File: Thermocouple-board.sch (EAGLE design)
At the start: 107 parts, among them J1 RJ45, J10 1X2-3.5MM, J11 1X2-3.5MM, J12 1X2-3.5MM, J13 1X2-3.5MM, J2 RJ45, J20 HEADER-1X1, J21 HEADER-1X1, J22 HEADER-1X1, J3 1981584-1LONGPADS, J4 2.1MMJACKTHM, J5 ST-LINK, J6 HEADER-1X3, J7 UART, SW1 PUSHBUTTON, SW2 PUSHBUTTON, U1 STM32F042K6, U10 MAX31855, U11 MAX31855, U12 MAX31855, U13 MAX31855, U20 EEPROM-I2C, U21 EEPROM-I2C, U30 ST3485, U31 ST3485, U40 LP298XS, U70 TPS25921, Y1 8MHz

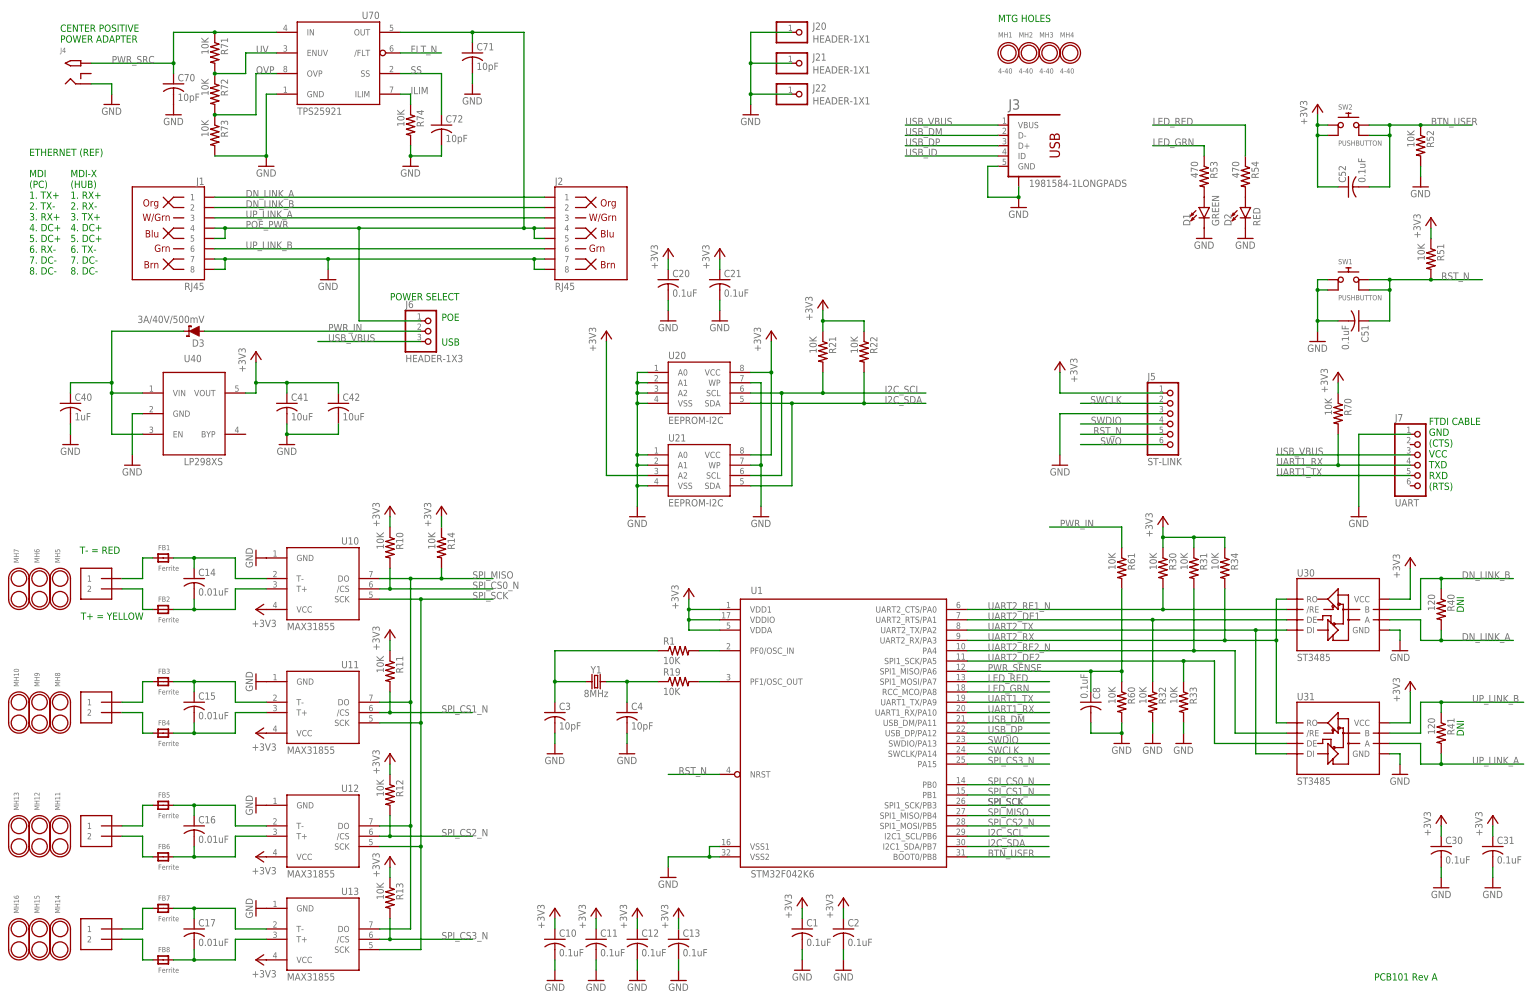
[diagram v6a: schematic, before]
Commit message: Update values on schematic
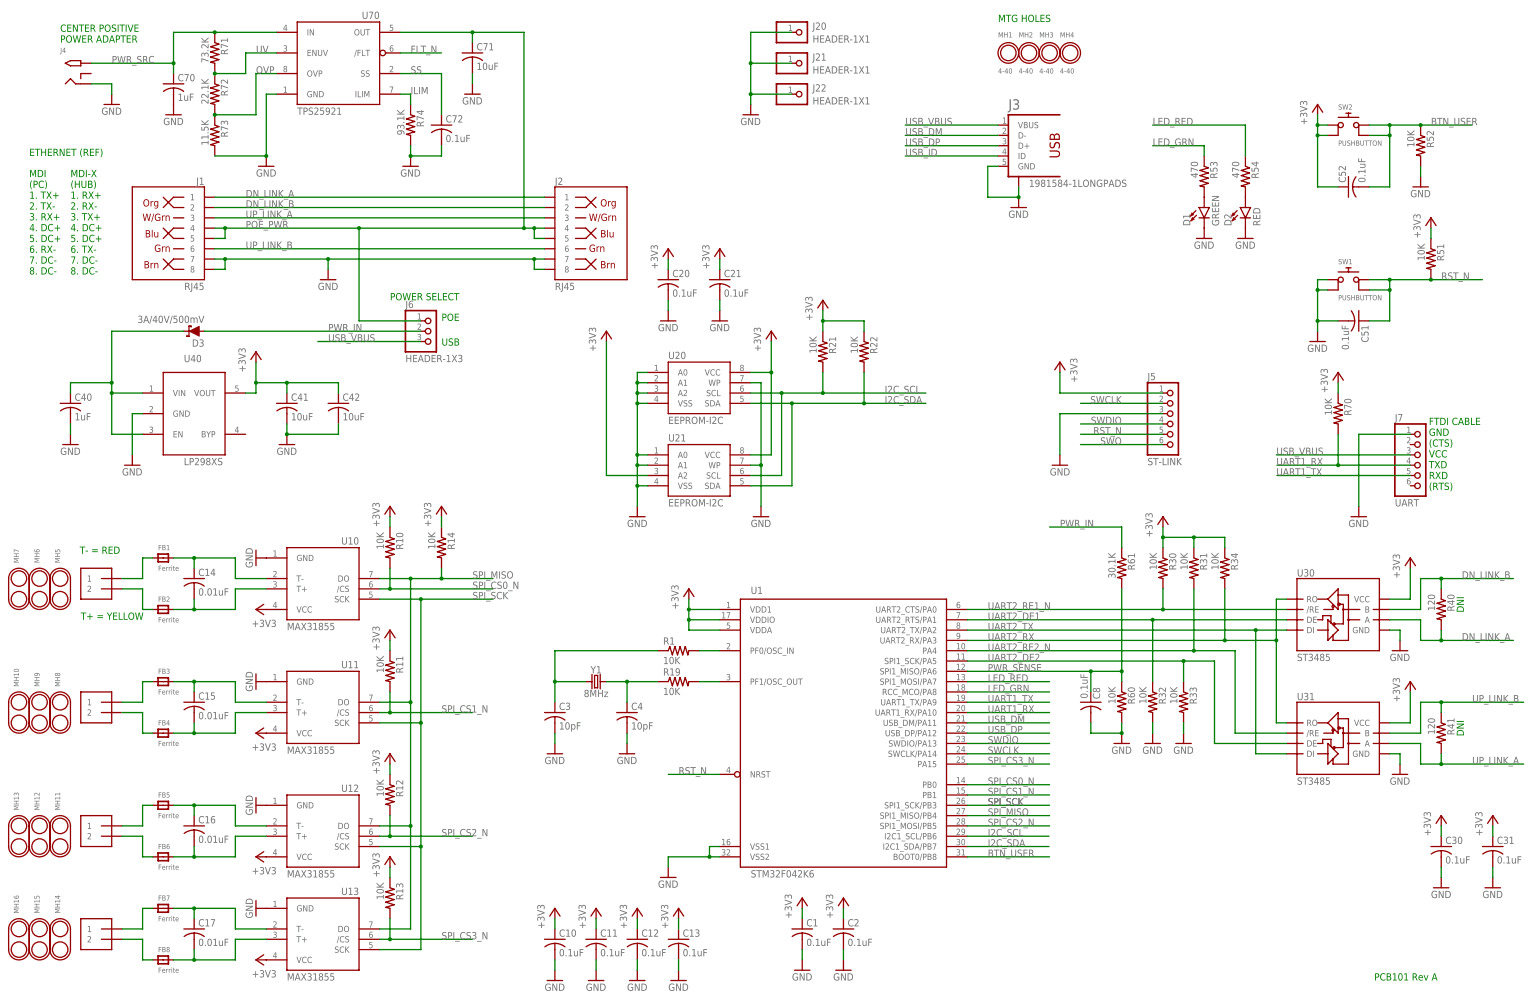
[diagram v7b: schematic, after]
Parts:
- C70: value 10pF -> 1uF
- C71: value 10pF -> 10uF
- C72: value 10pF -> 0.1uF
- R61: value 10K -> 30.1K
- R71: value 10K -> 73.2K
- R72: value 10K -> 22.1K
- R73: value 10K -> 11.5K
- R74: value 10K -> 93.1K
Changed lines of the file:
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@@
 <part name="MH4" library="Thermocouple-board" deviceset="MTG_HOLE" device="_4-40" value="4-40"/>
 <part name="R60" library="adafruit" deviceset="R-US_" device="R0805" value="10K"/>
-<part name="R61" library="adafruit" deviceset="R-US_" device="R0805" value="10K"/>
+<part name="R61" library="adafruit" deviceset="R-US_" device="R0805" value="30.1K"/>
 <part name="GND10" library="supply1" deviceset="GND" device=""/>
 <part name="C8" library="adafruit" library_urn="urn:adsk.eagle:library:420" deviceset="C-US" device="C0805K" package3d_urn="urn:adsk.eagle:package:6240397/1" value="0.1uF"/>
@@
 <part name="GND37" library="supply1" deviceset="GND" device=""/>
 <part name="GND38" library="supply1" deviceset="GND" device=""/>
-<part name="R71" library="adafruit" deviceset="R-US_" device="R0805" value="10K"/>
-<part name="R72" library="adafruit" deviceset="R-US_" device="R0805" value="10K"/>
-<part name="R73" library="adafruit" deviceset="R-US_" device="R0805" value="10K"/>
-<part name="R74" library="adafruit" deviceset="R-US_" device="R0805" value="10K"/>
-<part name="C72" library="adafruit" library_urn="urn:adsk.eagle:library:420" deviceset="C-US" device="C0805K" package3d_urn="urn:adsk.eagle:package:6240397/1" value="10pF"/>
-<part name="C71" library="adafruit" library_urn="urn:adsk.eagle:library:420" deviceset="C-US" device="C0805K" package3d_urn="urn:adsk.eagle:package:6240397/1" value="10pF"/>
+<part name="R71" library="adafruit" deviceset="R-US_" device="R0805" value="73.2K"/>
+<part name="R72" library="adafruit" deviceset="R-US_" device="R0805" value="22.1K"/>
+<part name="R73" library="adafruit" deviceset="R-US_" device="R0805" value="11.5K"/>
+<part name="R74" library="adafruit" deviceset="R-US_" device="R0805" value="93.1K"/>
+<part name="C72" library="adafruit" library_urn="urn:adsk.eagle:library:420" deviceset="C-US" device="C0805K" package3d_urn="urn:adsk.eagle:package:6240397/1" value="0.1uF"/>
+<part name="C71" library="adafruit" library_urn="urn:adsk.eagle:library:420" deviceset="C-US" device="C0805K" package3d_urn="urn:adsk.eagle:package:6240397/1" value="10uF"/>
 <part name="GND39" library="supply1" deviceset="GND" device=""/>
 <part name="R40" library="adafruit" deviceset="R-US_" device="R0805" value="120"/>
 <part name="R41" library="adafruit" deviceset="R-US_" device="R0805" value="120"/>
-<part name="C70" library="adafruit" library_urn="urn:adsk.eagle:library:420" deviceset="C-US" device="C0805K" package3d_urn="urn:adsk.eagle:package:6240397/1" value="10pF"/>
+<part name="C70" library="adafruit" library_urn="urn:adsk.eagle:library:420" deviceset="C-US" device="C0805K" package3d_urn="urn:adsk.eagle:package:6240397/1" value="1uF"/>
 <part name="GND40" library="supply1" deviceset="GND" device=""/>
 <part name="MH5" library="Thermocouple-board" deviceset="HOLD_DOWN" device=""/>
